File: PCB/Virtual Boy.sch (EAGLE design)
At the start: 21 parts, among them U1A SN74AHCT125N, U2A SN74AHCT125N, U3A SN74AHCT125N, U4A SN74AHCT125N

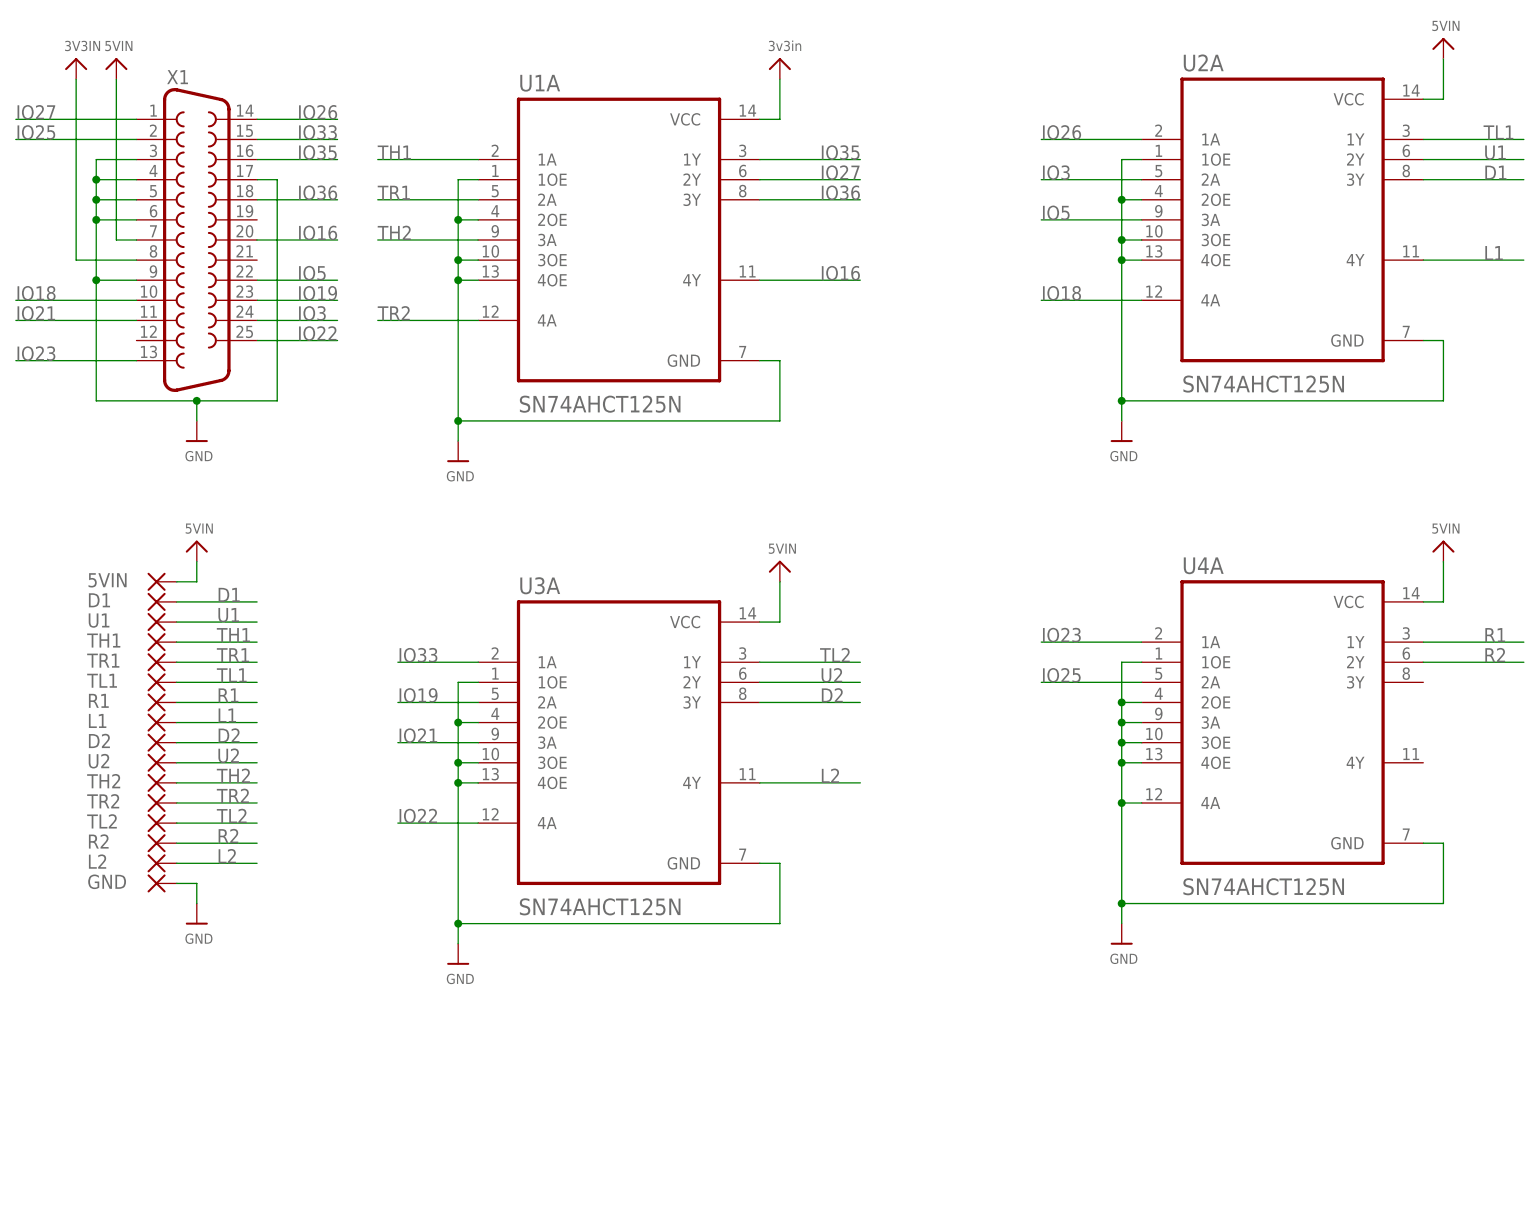
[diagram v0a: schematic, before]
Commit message: PCB Updates/New Additions
All existing PCBs had silkscreen updates and NES, Virtual Boy, PSX/PS2, Nintendo 64, Saturn have been added.
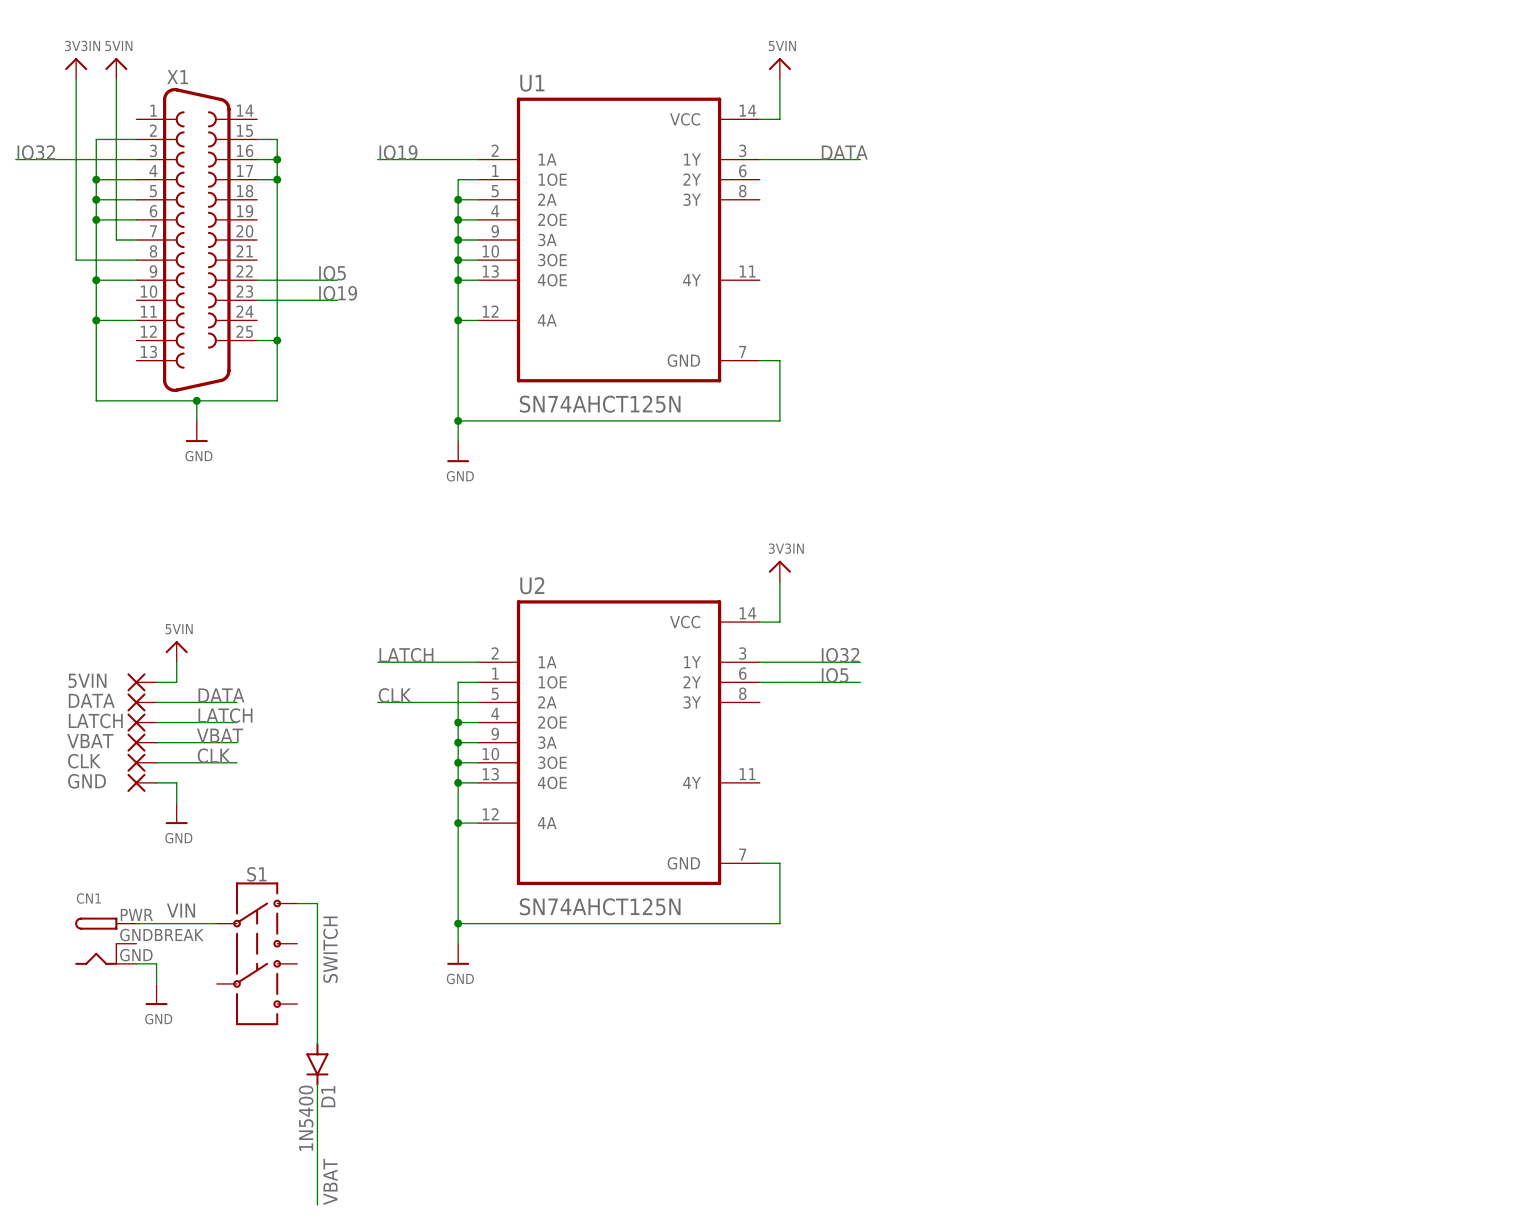
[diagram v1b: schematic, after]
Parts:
- removed D2, L1, L2, R1, R2, TH1, TH2, TL1, TL2, TR1, TR2: (no value), wirepad:SMD5
- removed U1A, U2A, U3A, U4A: SN74AHCT125N, SN74AHCT125N:SN74AHCT125N
- added CLK, DATA, LATCH, VBAT: (no value), wirepad:SMD5
- added CN1: (no value), adafruit:DCBARRELPTH
- added S1: (no value), Switch Mod:SWITCH-DPDT-PTH-GPI-152-3013
- D1: value (none) -> 1N5400; device wirepad:SMD5 -> diode:1N5400
- U1, U2: value (none) -> SN74AHCT125N; device wirepad:SMD5 -> SN74AHCT125N:SN74AHCT125N
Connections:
- removed net D1: D1.P, U2A.3Y
- removed net D2: D2.P, U3A.3Y
- removed net IO16: U1A.4Y, X1.20
- removed net IO18: U2A.4A, X1.10
- removed net IO21: U3A.3A, X1.11
- removed net IO22: U3A.4A, X1.25
- removed net IO23: U4A.1A, X1.13
- removed net IO25: U4A.2A, X1.2
- removed net IO26: U2A.1A, X1.14
- removed net IO27: U1A.2Y, X1.1
- removed net IO3: U2A.2A, X1.24
- removed net IO33: U3A.1A, X1.15
- removed net IO35: U1A.1Y, X1.16
- removed net IO36: U1A.3Y, X1.18
- removed net L1: L1.P, U2A.4Y
- removed net L2: L2.P, U3A.4Y
- removed net R1: R1.P, U4A.1Y
- removed net R2: R2.P, U4A.2Y
- removed net TH1: TH1.P, U1A.1A
- removed net TH2: TH2.P, U1A.3A
- removed net TL1: TL1.P, U2A.1Y
- removed net TL2: TL2.P, U3A.1Y
- removed net TR1: TR1.P, U1A.2A
- removed net TR2: TR2.P, U1A.4A
- removed net U1: U1.P, U2A.2Y
- removed net U2: U2.P, U3A.2Y
- new net CLK: CLK.P, U2.2A
- new net DATA: DATA.P, U1.1Y
- new net IO32: U2.1Y, X1.3
- new net LATCH: LATCH.P, U2.1A
- new net SWITCH: D1.A, S1.1
- new net VBAT: D1.C, VBAT.P
- new net VIN: CN1.PWR, S1.2
- net 3V3IN: now also U2.VCC; no longer U1A.VCC
- net 5VIN: now also U1.VCC; no longer U2A.VCC, U3A.VCC, U4A.VCC
- net GND: now also CN1.GND, U1.1OE, U1.2A, U1.2OE, U1.3A, U1.3OE, U1.4A, U1.4OE, U1.GND, U2.1OE, U2.2OE, U2.3A, U2.3OE, U2.4A, U2.4OE, U2.GND, X1.11, X1.15, X1.16, X1.2, X1.25; no longer U1A.1OE, U1A.2OE, U1A.3OE, U1A.4OE, U1A.GND, U2A.1OE, U2A.2OE, U2A.3OE, U2A.4OE, U2A.GND, U3A.1OE, U3A.2OE, U3A.3OE, U3A.4OE, U3A.GND, U4A.1OE, U4A.2OE, U4A.3A, U4A.3OE, U4A.4A, U4A.4OE, U4A.GND, X1.3
- net IO19: now also U1.1A; no longer U3A.2A
- net IO5: now also U2.2Y; no longer U2A.3A
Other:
- moved on the sheet: 5VIN, GND

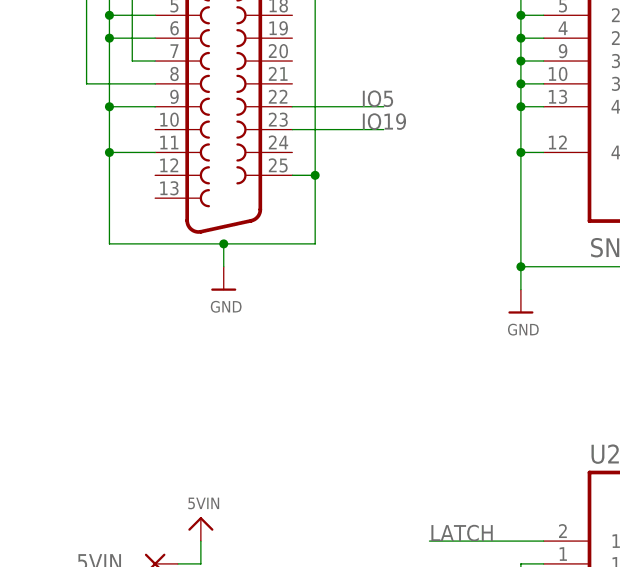
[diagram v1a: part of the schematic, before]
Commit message: Added exposed GND plane at DB25 anchors
All PCBs have been update to have exposed GND plane pads for the DB25 anchor points.

This resolves Issue 54
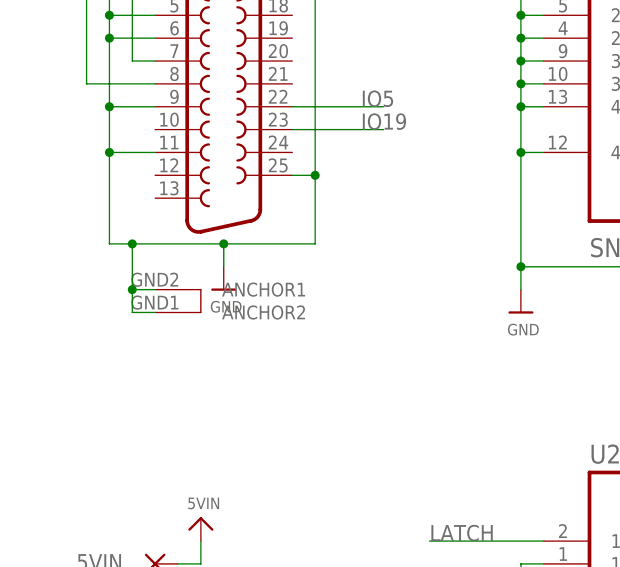
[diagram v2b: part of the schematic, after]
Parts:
- X1: device SparkFun-Retired:DB25_FEMALEH -> SparkFun-Retired:DB25_FEMALEHP
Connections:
- net GND: now also X1.ANCHOR1, X1.ANCHOR2
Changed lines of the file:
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@@
 </classes>
 <parts>
-<part name="X1" library="SparkFun-Retired" deviceset="DB25_FEMALE" device="H"/>
+<part name="X1" library="SparkFun-Retired" deviceset="DB25_FEMALE" device="HP"/>
 <part name="U$43" library="microbuilder" deviceset="VIN" device="" value="3V3IN"/>
 <part name="U$44" library="microbuilder" deviceset="VIN" device="" value="5VIN"/>
@@
 <segment>
 <wire x1="248.92" y1="-109.22" x2="238.76" y2="-109.22" width="0.1524" layer="91"/>
-<wire x1="238.76" y1="-109.22" x2="226.06" y2="-109.22" width="0.1524" layer="91"/>
+<wire x1="238.76" y1="-109.22" x2="228.6" y2="-109.22" width="0.1524" layer="91"/>
+<wire x1="228.6" y1="-109.22" x2="226.06" y2="-109.22" width="0.1524" layer="91"/>
 <wire x1="238.76" y1="-109.22" x2="238.76" y2="-111.76" width="0.1524" layer="91"/>
 <junction x="238.76" y="-109.22"/>
@@
 <wire x1="246.38" y1="-101.6" x2="248.92" y2="-101.6" width="0.1524" layer="91"/>
 <junction x="248.92" y="-101.6"/>
+<pinref part="X1" gate="-1" pin="ANCHOR2"/>
+<wire x1="231.14" y1="-116.84" x2="228.6" y2="-116.84" width="0.1524" layer="91"/>
+<wire x1="228.6" y1="-116.84" x2="228.6" y2="-114.3" width="0.1524" layer="91"/>
+<wire x1="228.6" y1="-114.3" x2="228.6" y2="-109.22" width="0.1524" layer="91"/>
+<pinref part="X1" gate="-1" pin="ANCHOR1"/>
+<wire x1="231.14" y1="-114.3" x2="228.6" y2="-114.3" width="0.1524" layer="91"/>
+<junction x="228.6" y="-114.3"/>
+<junction x="228.6" y="-109.22"/>
 </segment>
 <segment>
